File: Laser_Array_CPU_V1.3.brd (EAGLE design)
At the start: 104.1 x 109.6 mm, 72 parts, among them IC1 PIC24FJ64GA004, J1 MA16-2, J3 22-23-2021, J4 22-23-2021, J8 22-23-2021, U1 MAX6817, U2 LP2985-28DBVTE4, U4 LP2985-50DBVR, X1 22-23-2031, X2 22-23-2041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

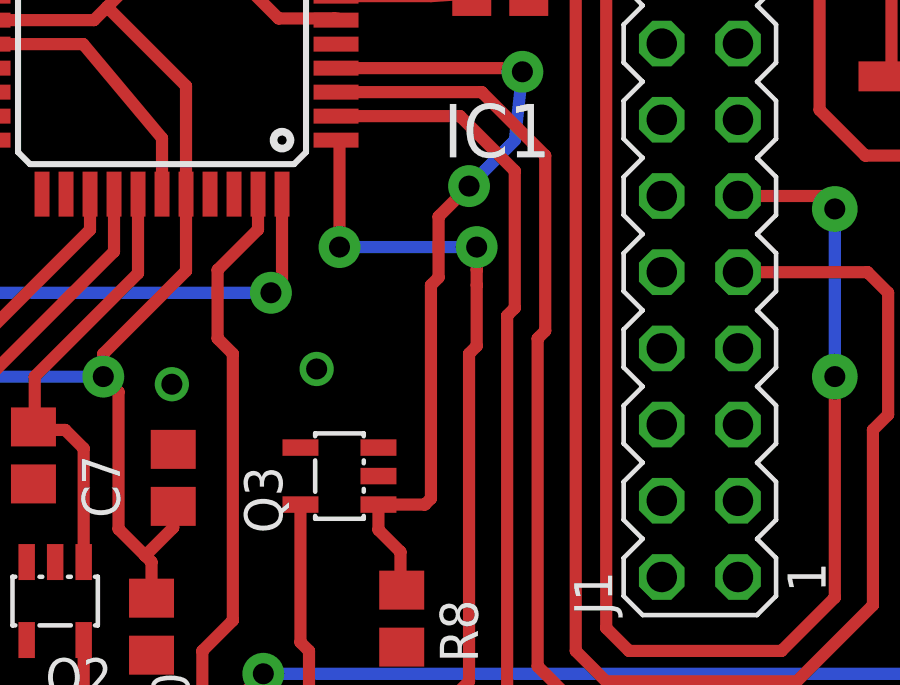
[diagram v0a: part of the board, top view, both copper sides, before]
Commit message: Finished Laser_Array next versions, all theee boards, Nov19_2018
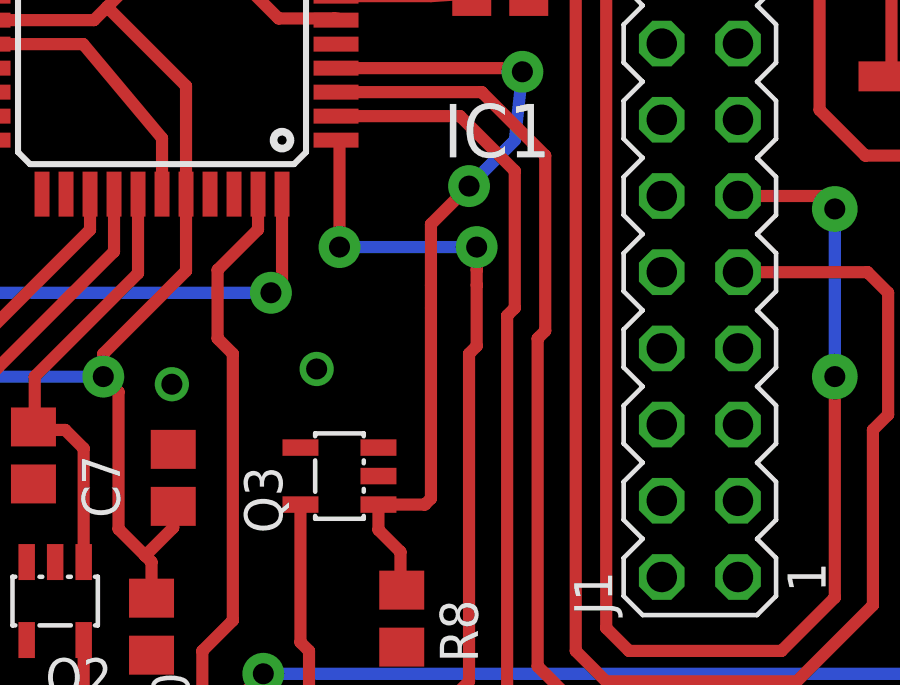
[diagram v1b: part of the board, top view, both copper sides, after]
